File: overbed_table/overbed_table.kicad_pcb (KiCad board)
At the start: 2 copper layers, 51 x 87.5 mm, 87 parts, among them CN10 DLL-5569-2AW, CN2 KF2EDGRC-5.08-4P, CN3 KF2EDGRC-5.08-4P, CN8 DLL-5569-2AW, CN9 DLL-5569-2AW, Q1 BSS138, Q2 BSS138, Q3 BSS138, Q4 AON7524, Q5 AON7524, Q6 AON7524, SW1 KH-6X6X6H-STM, SW2 KH-6X6X6H-STM, U1 AP2112K-3.3TRG1, U10 TPS562201DDCR, U11 TPS562201DDCR, U15 SP3485EN, U2 ESP32-C3-WROOM-02, U3 WAFER-XH254WZ-2A, U4 BSMD2920-500-24V, U5 BSMD2920-500-24V, U6 BSMD2920-500-24V, U7 KF7620-7.62-2P, X1 AFA01-S05FCA-00

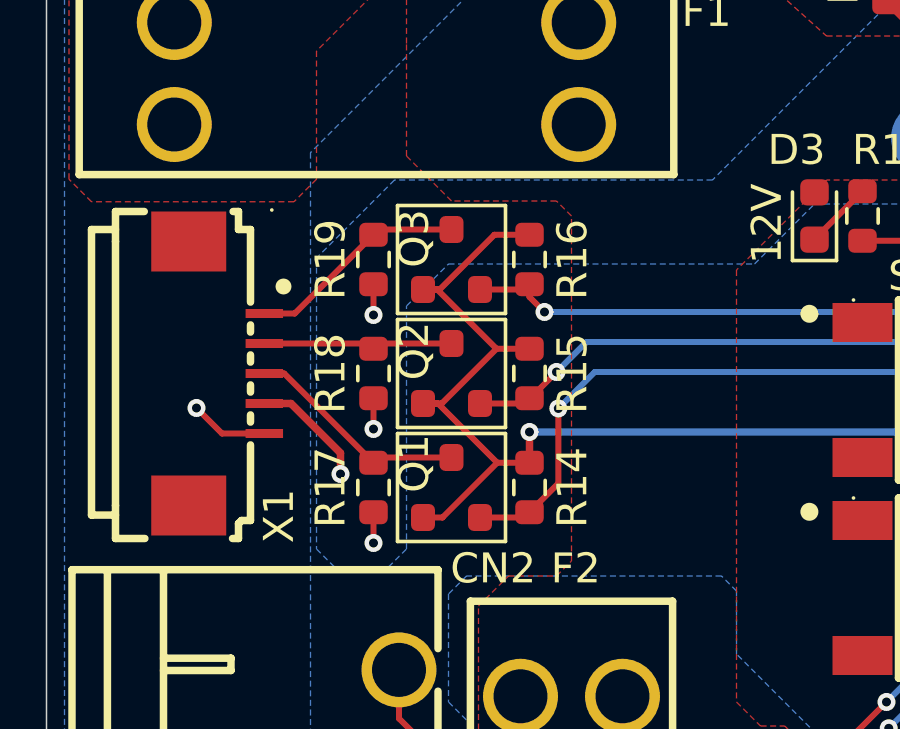
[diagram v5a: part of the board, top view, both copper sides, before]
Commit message: update: 更新按钮小板设计，导出gerber文件
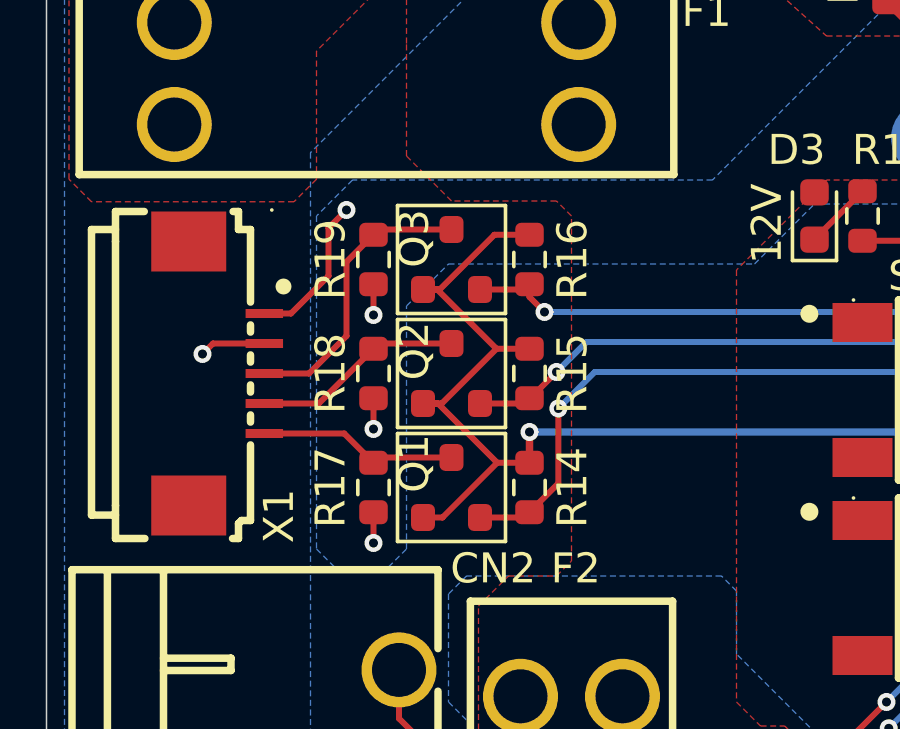
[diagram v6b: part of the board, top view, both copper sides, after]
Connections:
- X1 pad 1: /3V3_5V_转换器/5V_SIG2 -> /+5V
- X1 pad 2: /3V3_5V_转换器/5V_SIG1 -> /GND
- X1 pad 3: /3V3_5V_转换器/5V_SIG0 -> /3V3_5V_转换器/5V_SIG2
- X1 pad 4: /+5V -> /3V3_5V_转换器/5V_SIG1
- X1 pad 5: /GND -> /3V3_5V_转换器/5V_SIG0
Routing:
- net /3V3_5V_转换器/5V_SIG2: track 7.40 -> 9.68 mm
- net /+5V: track 29.3 -> 30.5 mm
- net /3V3_5V_转换器/5V_SIG0: track 7.54 -> 6.72 mm
- net /3V3_5V_转换器/5V_SIG1: track 6.38 -> 7.07 mm
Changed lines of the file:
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@@
 			(size 1.25 0.3)
 			(layers "F.Cu" "F.Mask" "F.Paste")
-			(net "/3V3_5V_转换器/5V_SIG2")
+			(net "/+5V")
 			(pinfunction "1_1")
 			(pintype "passive")
@@
 			(size 1.25 0.3)
 			(layers "F.Cu" "F.Mask" "F.Paste")
-			(net "/3V3_5V_转换器/5V_SIG1")
+			(net "/GND")
 			(pinfunction "2_2")
 			(pintype "passive")
@@
 			(size 1.25 0.3)
 			(layers "F.Cu" "F.Mask" "F.Paste")
-			(net "/3V3_5V_转换器/5V_SIG0")
+			(net "/3V3_5V_转换器/5V_SIG2")
 			(pinfunction "3_3")
 			(pintype "passive")
@@
 			(size 1.25 0.3)
 			(layers "F.Cu" "F.Mask" "F.Paste")
-			(net "/+5V")
+			(net "/3V3_5V_转换器/5V_SIG1")
 			(pinfunction "4_4")
 			(pintype "passive")
@@
 			(size 1.25 0.3)
 			(layers "F.Cu" "F.Mask" "F.Paste")
-			(net "/GND")
+			(net "/3V3_5V_转换器/5V_SIG0")
 			(pinfunction "5_5")
 			(pintype "passive")
@@
 	)
 	(segment
-		(start 30.85 62.25)
-		(end 30 61.4)
+		(start 32.26 59.25)
+		(end 30.55 59.25)
 		(width 0.2)
 		(layer "F.Cu")
@@
 	)
 	(segment
-		(start 32.26 62.25)
-		(end 30.85 62.25)
-		(width 0.2)
-		(layer "F.Cu")
-		(net "/GND")
-	)
-	(segment
 		(start 49.8 83.625)
 		(end 50.63 84.455)
@@
 	)
 	(segment
+		(start 30.55 59.25)
+		(end 30.2 59.6)
+		(width 0.2)
+		(layer "F.Cu")
+		(net "/GND")
+	)
+	(segment
 		(start 53.095 80.93)
 		(end 54.625 79.4)
@@
 	)
 	(via
+		(at 30.2 59.6)
+		(size 0.6)
+		(drill 0.3)
+		(layers "F.Cu" "B.Cu")
+		(net "/GND")
+	)
+	(via
 		(at 67.4 37)
 		(size 0.6)
@@
 	)
 	(via
-		(at 30 61.4)
-		(size 0.6)
-		(drill 0.3)
-		(layers "F.Cu" "B.Cu")
-		(net "/GND")
-	)
-	(via
 		(at 70.8 39.530513)
 		(size 1)
@@
 	)
 	(segment
-		(start 62 32.3875)
-		(end 61.4125 32.3875)
+		(start 35 54.8)
+		(end 34.4 55.4)
 		(width 0.2)
 		(layer "F.Cu")
@@
 	)
 	(segment
-		(start 33.15 61.25)
-		(end 34.8 62.9)
-		(width 0.25)
+		(start 62 32.3875)
+		(end 61.4125 32.3875)
+		(width 0.2)
 		(layer "F.Cu")
 		(net "/+5V")
 	)
 	(segment
-		(start 34.8 62.9)
-		(end 34.8 63.6)
-		(width 0.25)
+		(start 34.4 55.4)
+		(end 34.4 57)
+		(width 0.2)
 		(layer "F.Cu")
 		(net "/+5V")
@@
 	)
 	(segment
-		(start 32.26 61.25)
-		(end 33.15 61.25)
-		(width 0.25)
-		(layer "F.Cu")
-		(net "/+5V")
-	)
-	(segment
 		(start 35.9 62.1)
 		(end 35.9 61.075)
@@
 	)
 	(segment
+		(start 34.4 57)
+		(end 33.15 58.25)
+		(width 0.2)
+		(layer "F.Cu")
+		(net "/+5V")
+	)
+	(segment
 		(start 60.3 44.1)
 		(end 55.825 48.575)
@@
 		(net "/+5V")
 	)
+	(segment
+		(start 33.15 58.25)
+		(end 32.26 58.25)
+		(width 0.2)
+		(layer "F.Cu")
+		(net "/+5V")
+	)
 	(via
 		(at 35.9 62.1)
@@
 	)
 	(via
-		(at 34.8 63.6)
+		(at 35 54.8)
 		(size 0.6)
 		(drill 0.3)
@@
 	)
 	(segment
-		(start 32.925 60.25)
-		(end 35.9 63.225)
+		(start 38.5 63.05)
+		(end 36.075 63.05)
 		(width 0.2)
 		(layer "F.Cu")
@@
 	)
 	(segment
-		(start 38.5 63.05)
-		(end 36.075 63.05)
+		(start 32.26 62.25)
+		(end 34.925 62.25)
 		(width 0.2)
 		(layer "F.Cu")
@@
 	)
 	(segment
-		(start 32.26 60.25)
-		(end 32.925 60.25)
+		(start 34.925 62.25)
+		(end 35.9 63.225)
 		(width 0.2)
 		(layer "F.Cu")
@@
 	)
 	(segment
-		(start 32.26 59.25)
-		(end 35.725 59.25)
+		(start 32.26 61.25)
+		(end 34.075 61.25)
 		(width 0.2)
 		(layer "F.Cu")
@@
 	)
 	(segment
-		(start 36.075 59.25)
+		(start 34.075 61.25)
 		(end 35.9 59.425)
 		(width 0.2)
@@
 	)
 	(segment
-		(start 35.725 59.25)
+		(start 36.075 59.25)
 		(end 35.9 59.425)
 		(width 0.2)
@@
 	)
 	(segment
-		(start 33.275 58.25)
-		(end 35.9 55.625)
+		(start 33.75 60.25)
+		(end 35 59)
+		(width 0.2)
+		(layer "F.Cu")
+		(net "/3V3_5V_转换器/5V_SIG2")
+	)
+	(segment
+		(start 35 59)
+		(end 35 56.525)
 		(width 0.2)
 		(layer "F.Cu")
@@
 	)
 	(segment
-		(start 32.26 58.25)
-		(end 33.275 58.25)
+		(start 32.26 60.25)
+		(end 33.75 60.25)
 		(width 0.2)
 		(layer "F.Cu")
@@
 		(net "/3V3_5V_转换器/5V_SIG2")
 	)
+	(segment
+		(start 35 56.525)
+		(end 35.9 55.625)
+		(width 0.2)
+		(layer "F.Cu")
+		(net "/3V3_5V_转换器/5V_SIG2")
+	)
 	(zone
 		(net "/+12V")
@@
 			(pts
 				(xy 57.4 31.6) (xy 57.1 31.9) (xy 57.1 33.7) (xy 60.3 36.9) (xy 60.3 39.6) (xy 58.6 41.3) (xy 58.6 42.4)
-				(xy 47.2 53.8) (xy 36.6 53.8) (xy 34 56.4) (xy 34 66.1) (xy 34.6 66.7) (xy 36.4 66.7) (xy 37 66.1)
+				(xy 47.2 53.8) (xy 35.2 53.8) (xy 34 55) (xy 34 66.1) (xy 34.6 66.7) (xy 36.4 66.7) (xy 37 66.1)
 				(xy 37 58) (xy 38.4 56.6) (xy 48.6 56.6) (xy 50.6 54.6) (xy 55.2 54.6) (xy 56.8 53) (xy 56.8 48.4)
 				(xy 62.6 42.6) (xy 62.6 33.1) (xy 61.1 31.6)
